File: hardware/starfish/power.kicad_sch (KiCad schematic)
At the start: 28 parts, among them J201 DC in, J202 DC thru, Q201 DMP3037LSS-13, U201 VX7805-500, U202 MIC5317-3.3

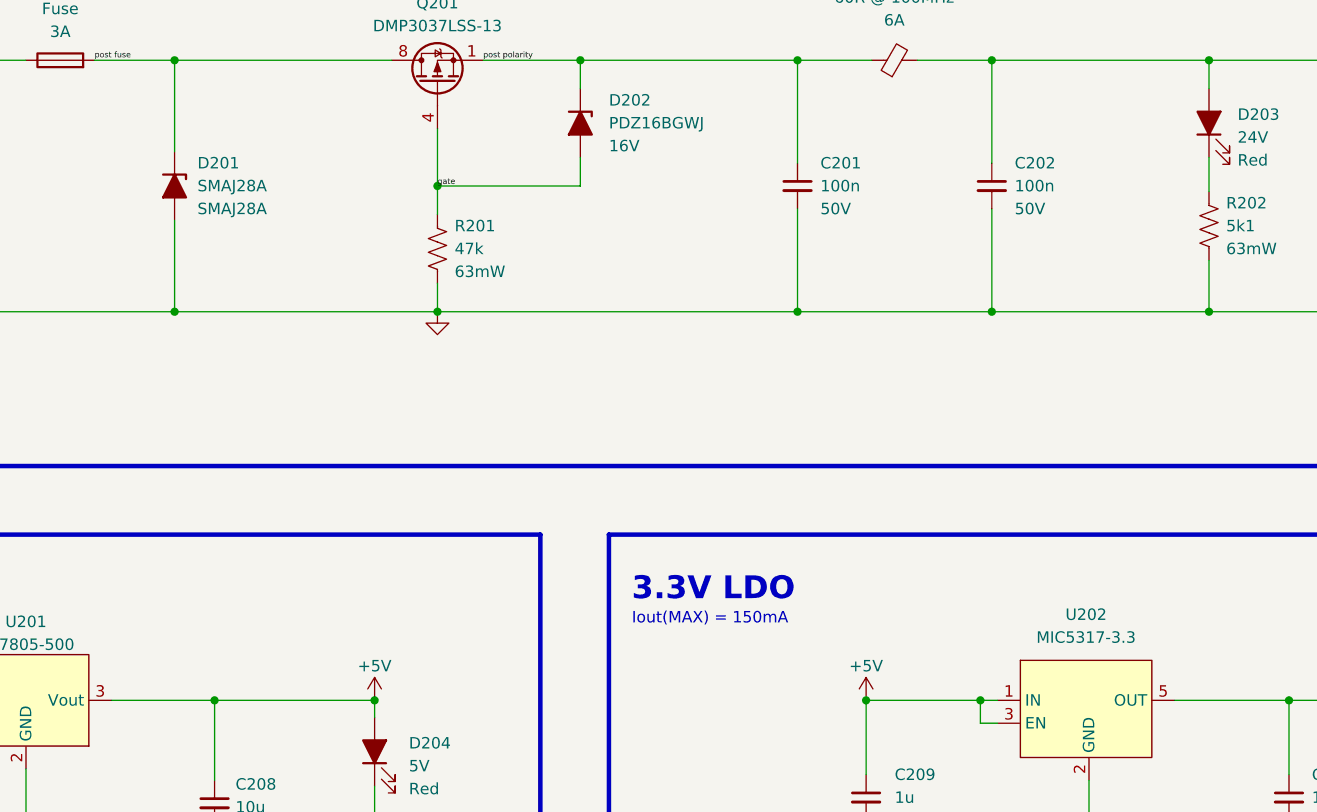
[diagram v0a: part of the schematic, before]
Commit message: starfish: fix diode values
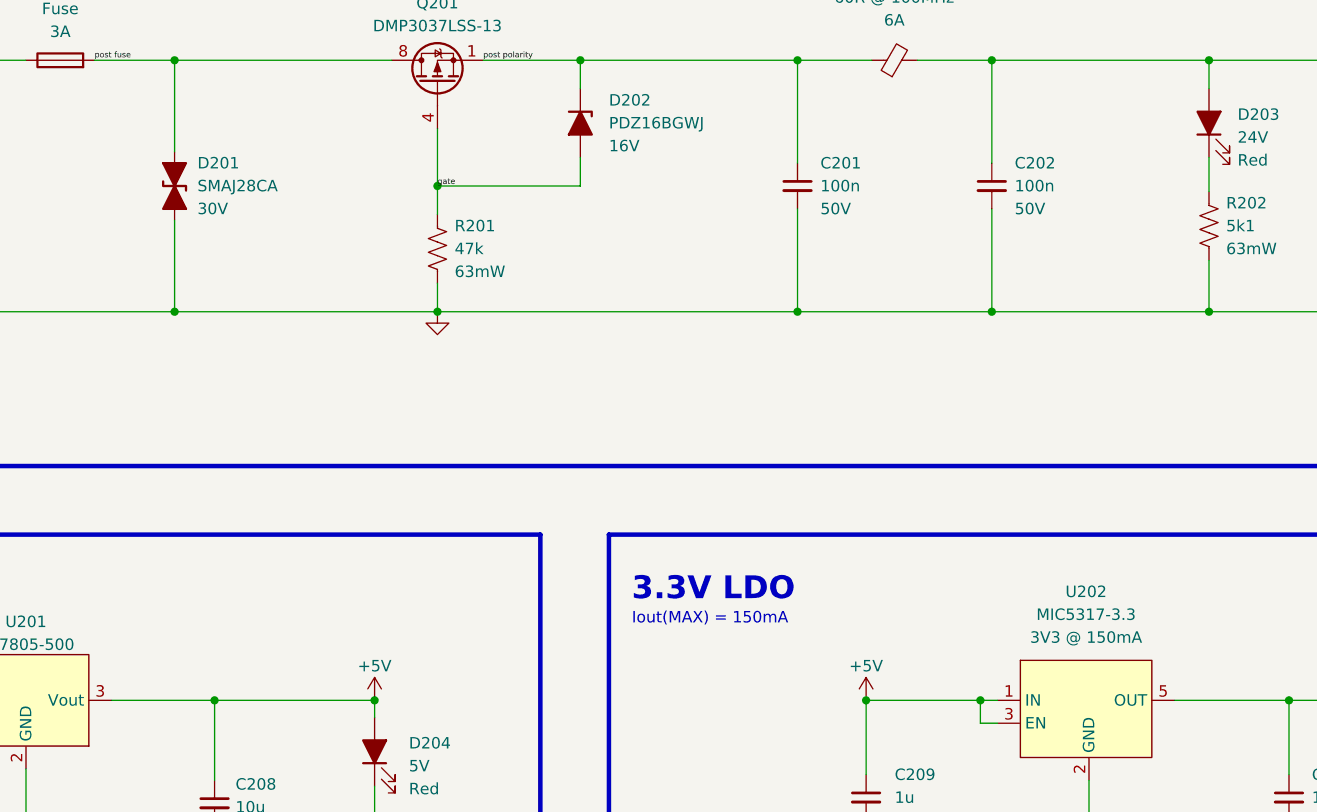
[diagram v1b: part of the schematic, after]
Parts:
- D201: value SMAJ28A -> SMAJ28CA; symbol Device:D_Zener_Filled -> Device:D_TVS_Filled; mpn SMAJ28A -> SMAJ28CA
- U202: Rating (none) -> 3V3 @ 150mA
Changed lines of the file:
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@@
     (pin "1")
   )
-  (symbol (lib_id "Device:D_Zener_Filled") (at 92.71 55.245 270) (unit 1)
+  (symbol (lib_id "Device:D_TVS_Filled") (at 92.71 55.245 270) (unit 1)
     (in_bom yes) (on_board yes) (fields_autoplaced)
     (property "Reference" "D201" (id 0) (at 95.25 52.7049 90)
       (effects (font (size 1.27 1.27)) (justify left))
     )
-    (property "Value" "SMAJ28A" (id 1) (at 95.25 55.2449 90)
+    (property "Value" "SMAJ28CA" (id 1) (at 95.25 55.2449 90)
       (effects (font (size 1.27 1.27)) (justify left))
     )
@@
       (effects (font (size 1.27 1.27)) hide)
     )
-    (property "Datasheet" "~" (id 3) (at 92.71 55.245 0)
-      (effects (font (size 1.27 1.27)) hide)
-    )
-    (property "Rating" "30V" (id 4) (at 92.71 55.245 90)
-      (effects (font (size 1.27 1.27)) hide)
-    )
-    (property "mpn" "SMAJ28A" (id 5) (at 95.25 57.7849 90)
-      (effects (font (size 1.27 1.27)) (justify left))
+    (property "Datasheet" "https://www.littelfuse.com/~/media/electronics/datasheets/tvs_diodes/littelfuse_tvs_diode_smaj_datasheet.pdf.pdf" (id 3) (at 92.71 55.245 0)
+      (effects (font (size 1.27 1.27)) hide)
+    )
+    (property "Rating" "30V" (id 4) (at 95.25 57.7849 90)
+      (effects (font (size 1.27 1.27)) (justify left))
+    )
+    (property "mpn" "SMAJ28CA" (id 5) (at 95.25 57.7849 90)
+      (effects (font (size 1.27 1.27)) (justify left) hide)
     )
     (pin "1")
@@
   )
   (symbol (lib_id "Device:LED_Filled") (at 207.645 48.26 90) (unit 1)
-    (in_bom yes) (on_board yes) (fields_autoplaced)
+    (in_bom yes) (on_board yes)
     (property "Reference" "D203" (id 0) (at 210.82 47.3074 90)
       (effects (font (size 1.27 1.27)) (justify right))
@@
   (symbol (lib_id "winterbloom:MIC5317") (at 194.31 112.395 0) (unit 1)
     (in_bom yes) (on_board yes) (fields_autoplaced)
-    (property "Reference" "U202" (id 0) (at 193.9925 102.87 0))
-    (property "Value" "MIC5317-3.3" (id 1) (at 193.9925 105.41 0))
+    (property "Reference" "U202" (id 0) (at 193.9925 100.33 0))
+    (property "Value" "MIC5317-3.3" (id 1) (at 193.9925 102.87 0))
     (property "Footprint" "Package_TO_SOT_SMD:SOT-23-5" (id 2) (at 194.31 103.505 0)
       (effects (font (size 1.27 1.27)) hide)
@@
       (effects (font (size 1.27 1.27)) hide)
     )
-    (pin "1")
-    (pin "2")
+    (property "Rating" "3V3 @ 150mA" (id 5) (at 193.9925 105.41 0))
+    (pin "1")
+    (pin "2")
